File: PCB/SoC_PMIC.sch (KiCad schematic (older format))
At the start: 1 part

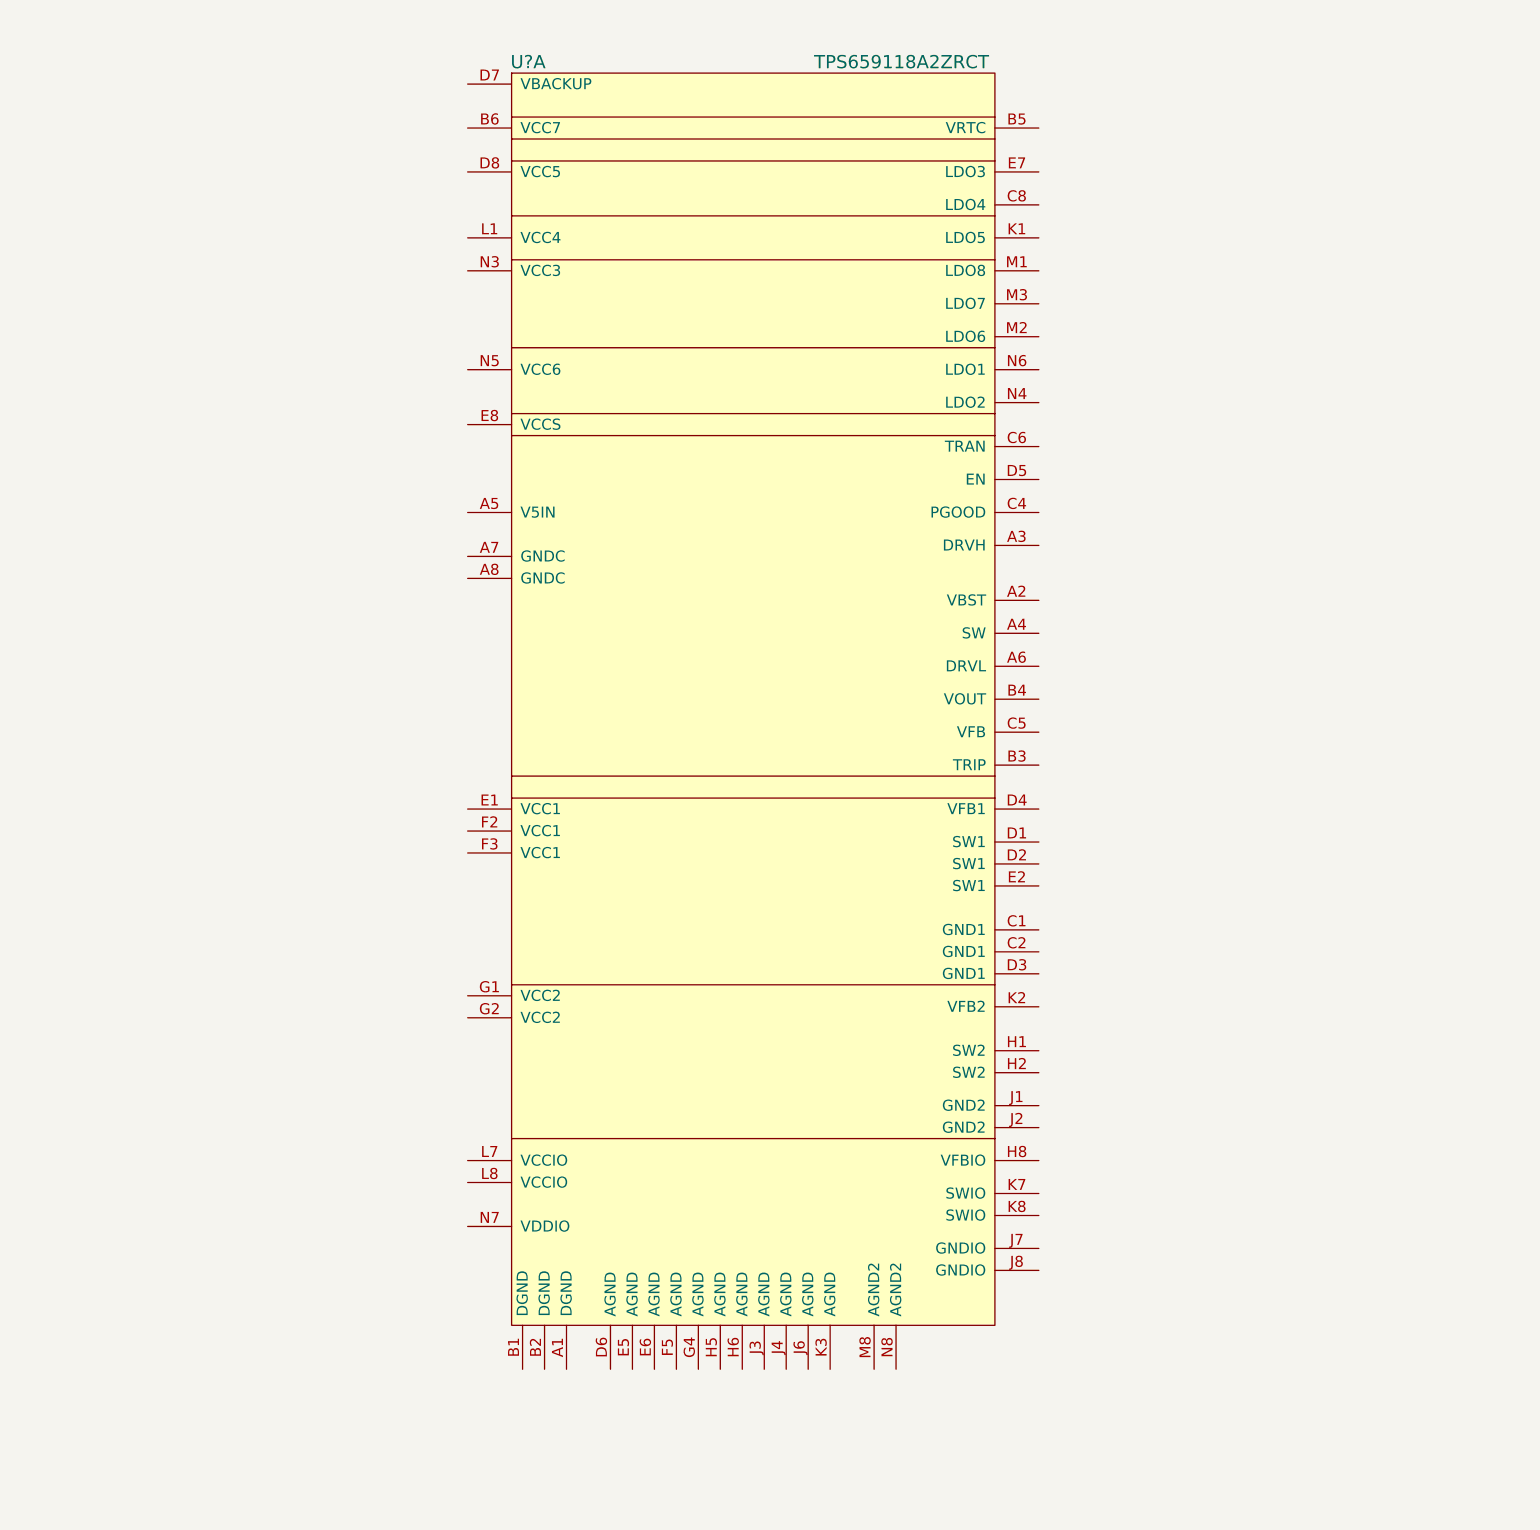
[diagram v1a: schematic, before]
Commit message: Cam / PMIC
Camera data bus entry relabled, PMIC started.
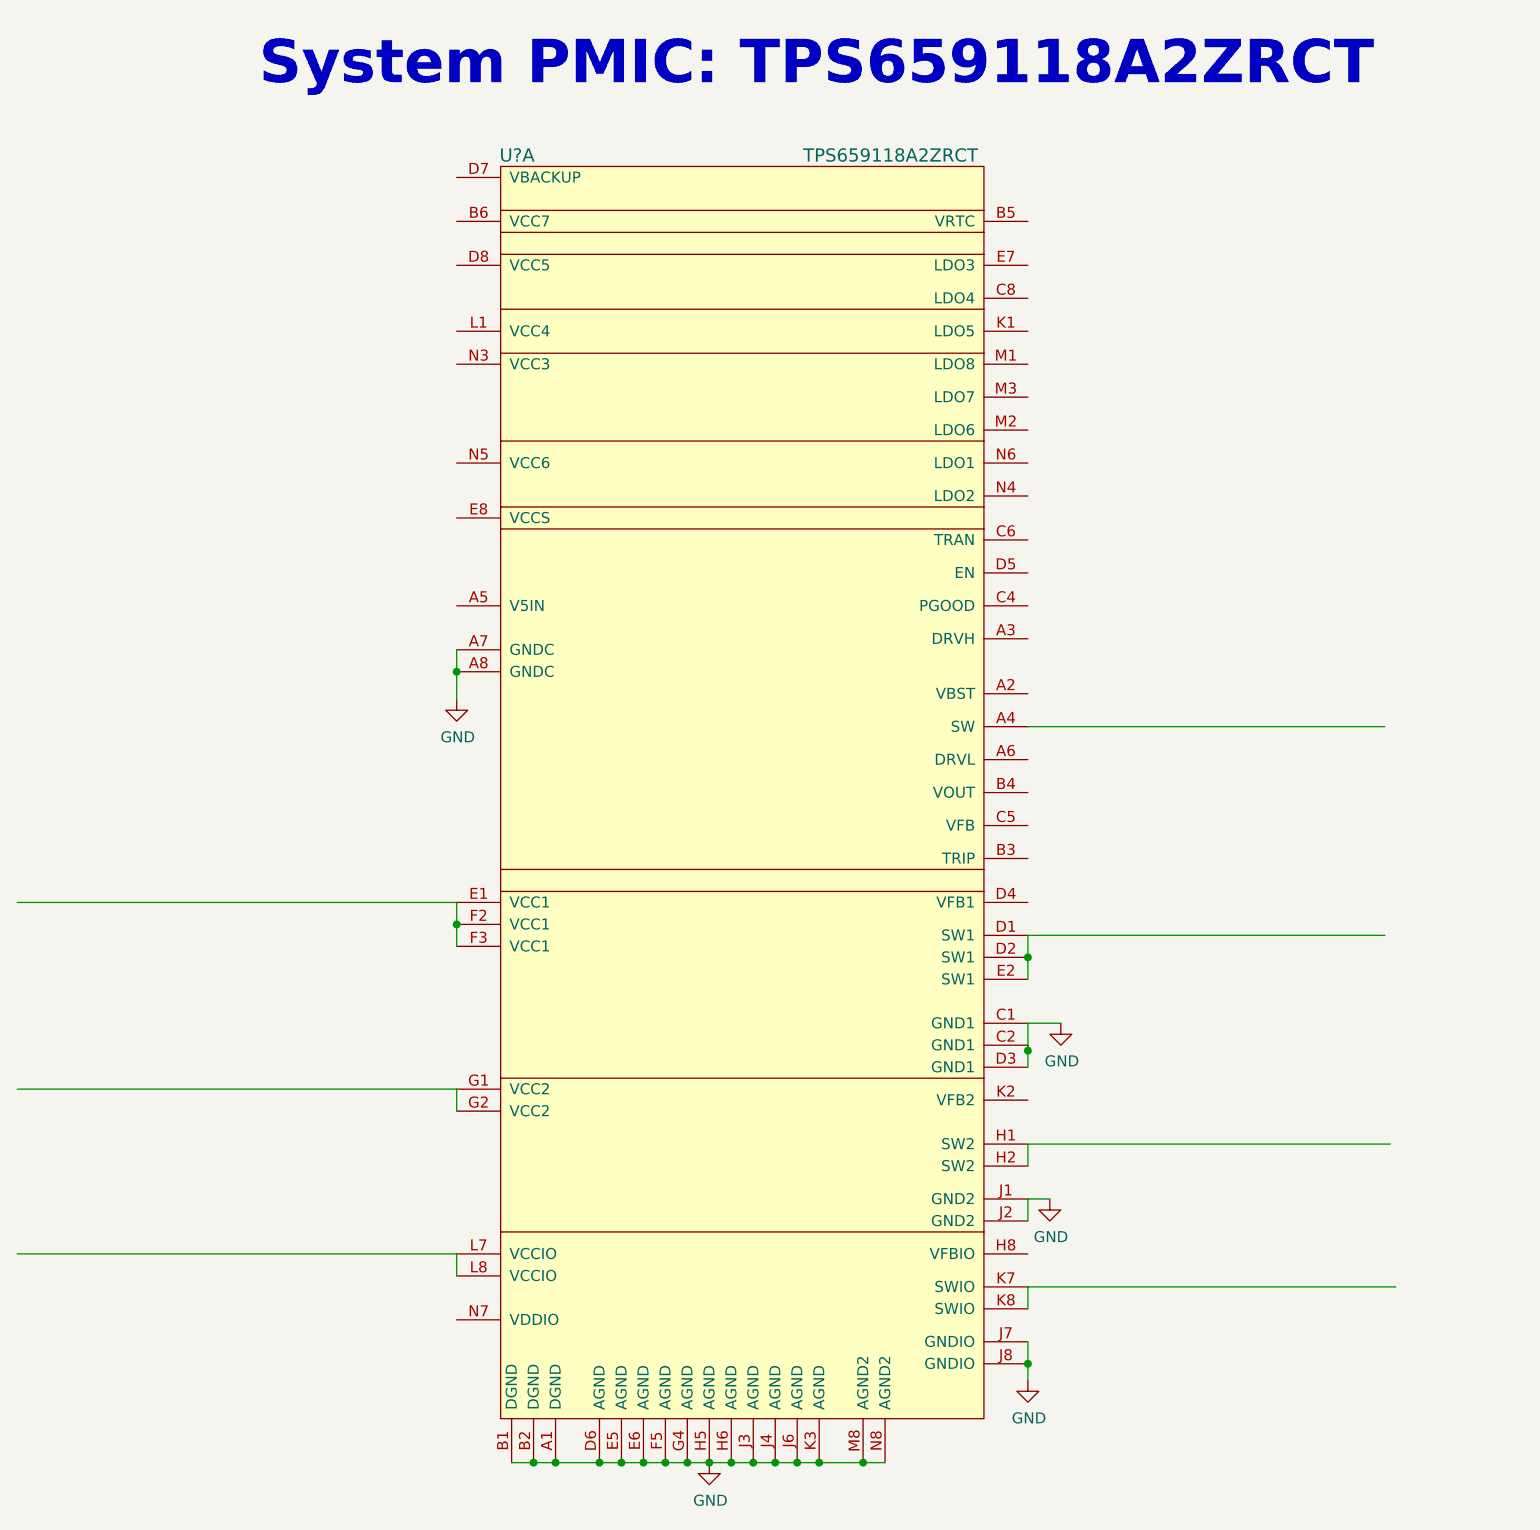
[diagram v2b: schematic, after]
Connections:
- net labels added: GND
- wire segments 0 -> 21
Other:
- note added: "System PMIC: TPS659118A2ZRCT"
- moved on the sheet: U?A
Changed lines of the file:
@@
 L TPS659118A2ZRCT U?
 U 1 1 58787CF1
-P 5625 3675
-F 0 "U?" H 4600 6625 60  0000 C CNN
-F 1 "TPS659118A2ZRCT" H 6300 6625 60  0000 C CNN
-F 2 "PCB_Footprints:TPS659118A2ZRCT" H 6250 8450 60  0001 C CNN
-F 3 "http://www.ti.com/lit/ds/symlink/tps65911.pdf" H 6450 8575 60  0001 C CNN
-F 4 "9.51000" H 4675 6725 60  0001 C CNN "Cost"
-F 5 "12 Jan 2017" H 4775 6825 60  0001 C CNN "Date Created"
-F 6 "12 Jan 2017" H 4875 6925 60  0001 C CNN "Date Modified"
-F 7 "Adam Vadala-Roth" H 4975 7025 60  0001 C CNN "Designer"
-F 8 "0.77mm" H 5075 7125 60  0001 C CNN "Height"
-F 9 "Yes" H 5175 7225 60  0001 C CNN "RhoS?"
-F 10 "Texas Instruments" H 5275 7325 60  0001 C CNN "MFR"
-F 11 "TPS659118A2ZRCT" H 5375 7425 60  0001 C CNN "MFR#"
-F 12 "SMT/SMD" H 5475 7525 60  0001 C CNN "Mounting"
-F 13 "98" H 5575 7625 60  0001 C CNN "Pin Count#"
-F 14 "Active" H 5675 7725 60  0001 C CNN "Status"
-F 15 "N/A" H 5775 7825 60  0001 C CNN "Tolerance"
-F 16 "IC PMIC DC/DC LDO 98BGA" H 5875 7925 60  0001 C CNN "Type"
-F 17 "2.7-5.5V" H 5975 8025 60  0001 C CNN "Voltage"
-F 18 "N/A" H 6075 8125 60  0001 C CNN "Wattage"
-F 19 "N/A" H 6175 8225 60  0001 C CNN "Component-Value"
-F 20 "Portable Equipment PMIC 98-BGA Microstar JR" H 6275 8325 60  0001 C CNN "Description"
-	1    5625 3675
+P 5575 4100
+F 0 "U?" H 4550 7050 60  0000 C CNN
+F 1 "TPS659118A2ZRCT" H 6250 7050 60  0000 C CNN
+F 2 "PCB_Footprints:TPS659118A2ZRCT" H 6200 8875 60  0001 C CNN
+F 3 "http://www.ti.com/lit/ds/symlink/tps65911.pdf" H 6400 9000 60  0001 C CNN
+F 4 "9.51000" H 4625 7150 60  0001 C CNN "Cost"
+F 5 "12 Jan 2017" H 4725 7250 60  0001 C CNN "Date Created"
+F 6 "12 Jan 2017" H 4825 7350 60  0001 C CNN "Date Modified"
+F 7 "Adam Vadala-Roth" H 4925 7450 60  0001 C CNN "Designer"
+F 8 "0.77mm" H 5025 7550 60  0001 C CNN "Height"
+F 9 "Yes" H 5125 7650 60  0001 C CNN "RhoS?"
+F 10 "Texas Instruments" H 5225 7750 60  0001 C CNN "MFR"
+F 11 "TPS659118A2ZRCT" H 5325 7850 60  0001 C CNN "MFR#"
+F 12 "SMT/SMD" H 5425 7950 60  0001 C CNN "Mounting"
+F 13 "98" H 5525 8050 60  0001 C CNN "Pin Count#"
+F 14 "Active" H 5625 8150 60  0001 C CNN "Status"
+F 15 "N/A" H 5725 8250 60  0001 C CNN "Tolerance"
+F 16 "IC PMIC DC/DC LDO 98BGA" H 5825 8350 60  0001 C CNN "Type"
+F 17 "2.7-5.5V" H 5925 8450 60  0001 C CNN "Voltage"
+F 18 "N/A" H 6025 8550 60  0001 C CNN "Wattage"
+F 19 "N/A" H 6125 8650 60  0001 C CNN "Component-Value"
+F 20 "Portable Equipment PMIC 98-BGA Microstar JR" H 6225 8750 60  0001 C CNN "Description"
+	1    5575 4100
 	1    0    0    -1
 $EndComp
+Wire Wire Line
+	4525 7100 6225 7100
+Connection ~ 4625 7100
+Connection ~ 4725 7100
+Connection ~ 4925 7100
+Connection ~ 5025 7100
+Connection ~ 5125 7100
+Connection ~ 5225 7100
+Connection ~ 5325 7100
+Connection ~ 5425 7100
+Connection ~ 5525 7100
+Connection ~ 5625 7100
+Connection ~ 5725 7100
+Connection ~ 5825 7100
+Connection ~ 5925 7100
+Connection ~ 6125 7100
+Wire Wire Line
+	6875 6550 6875 6725
+Wire Wire Line
+	6875 6000 6875 5900
+Wire Wire Line
+	6875 5200 6875 5300
+Wire Wire Line
+	6875 5225 6875 5100
+Connection ~ 6875 5225
+Wire Wire Line
+	4275 3400 4275 3625
+$Comp
+L GND #PWR?
+U 1 1 587D03A3
+P 5425 7100
+F 0 "#PWR?" H 5425 6850 50  0001 C CNN
+F 1 "GND" H 5430 6927 50  0000 C CNN
+F 2 "" H 5425 7100 50  0000 C CNN
+F 3 "" H 5425 7100 50  0000 C CNN
+	1    5425 7100
+	1    0    0    -1
+$EndComp
+$Comp
+L GND #PWR?
+U 1 1 587D03CF
+P 6875 6725
+F 0 "#PWR?" H 6875 6475 50  0001 C CNN
+F 1 "GND" H 6880 6552 50  0000 C CNN
+F 2 "" H 6875 6725 50  0000 C CNN
+F 3 "" H 6875 6725 50  0000 C CNN
+	1    6875 6725
+	1    0    0    -1
+$EndComp
+Connection ~ 6875 6650
+$Comp
+L GND #PWR?
+U 1 1 587D040E
+P 6975 5900
+F 0 "#PWR?" H 6975 5650 50  0001 C CNN
+F 1 "GND" H 6980 5727 50  0000 C CNN
+F 2 "" H 6975 5900 50  0000 C CNN
+F 3 "" H 6975 5900 50  0000 C CNN
+	1    6975 5900
+	1    0    0    -1
+$EndComp
+Wire Wire Line
+	6875 5900 6975 5900
+$Comp
+L GND #PWR?
+U 1 1 587D0455
+P 7025 5100
+F 0 "#PWR?" H 7025 4850 50  0001 C CNN
+F 1 "GND" H 7030 4927 50  0000 C CNN
+F 2 "" H 7025 5100 50  0000 C CNN
+F 3 "" H 7025 5100 50  0000 C CNN
+	1    7025 5100
+	1    0    0    -1
+$EndComp
+Wire Wire Line
+	6875 5100 7025 5100
+$Comp
+L GND #PWR?
+U 1 1 587D04A5
+P 4275 3625
+F 0 "#PWR?" H 4275 3375 50  0001 C CNN
+F 1 "GND" H 4280 3452 50  0000 C CNN
+F 2 "" H 4275 3625 50  0000 C CNN
+F 3 "" H 4275 3625 50  0000 C CNN
+	1    4275 3625
+	1    0    0    -1
+$EndComp
+Connection ~ 4275 3500
+Wire Wire Line
+	6875 5750 6875 5650
+Wire Wire Line
+	6875 5650 8525 5650
+Wire Wire Line
+	6875 6300 6875 6400
+Wire Wire Line
+	6875 6300 8550 6300
+Wire Wire Line
+	6875 4700 6875 4900
+Connection ~ 6875 4800
+Wire Wire Line
+	6875 4700 8500 4700
+Wire Wire Line
+	6875 3750 8500 3750
+Text Notes 3375 850  0    197  ~ 39
+System PMIC: TPS659118A2ZRCT
+Wire Wire Line
+	4275 4550 4275 4750
+Connection ~ 4275 4650
+Wire Wire Line
+	4275 5400 4275 5500
+Wire Wire Line
+	4275 6150 4275 6250
+Wire Wire Line
+	4275 6150 2275 6150
+Wire Wire Line
+	4275 5400 2275 5400
+Wire Wire Line
+	4275 4550 2275 4550
 $EndSCHEMATC

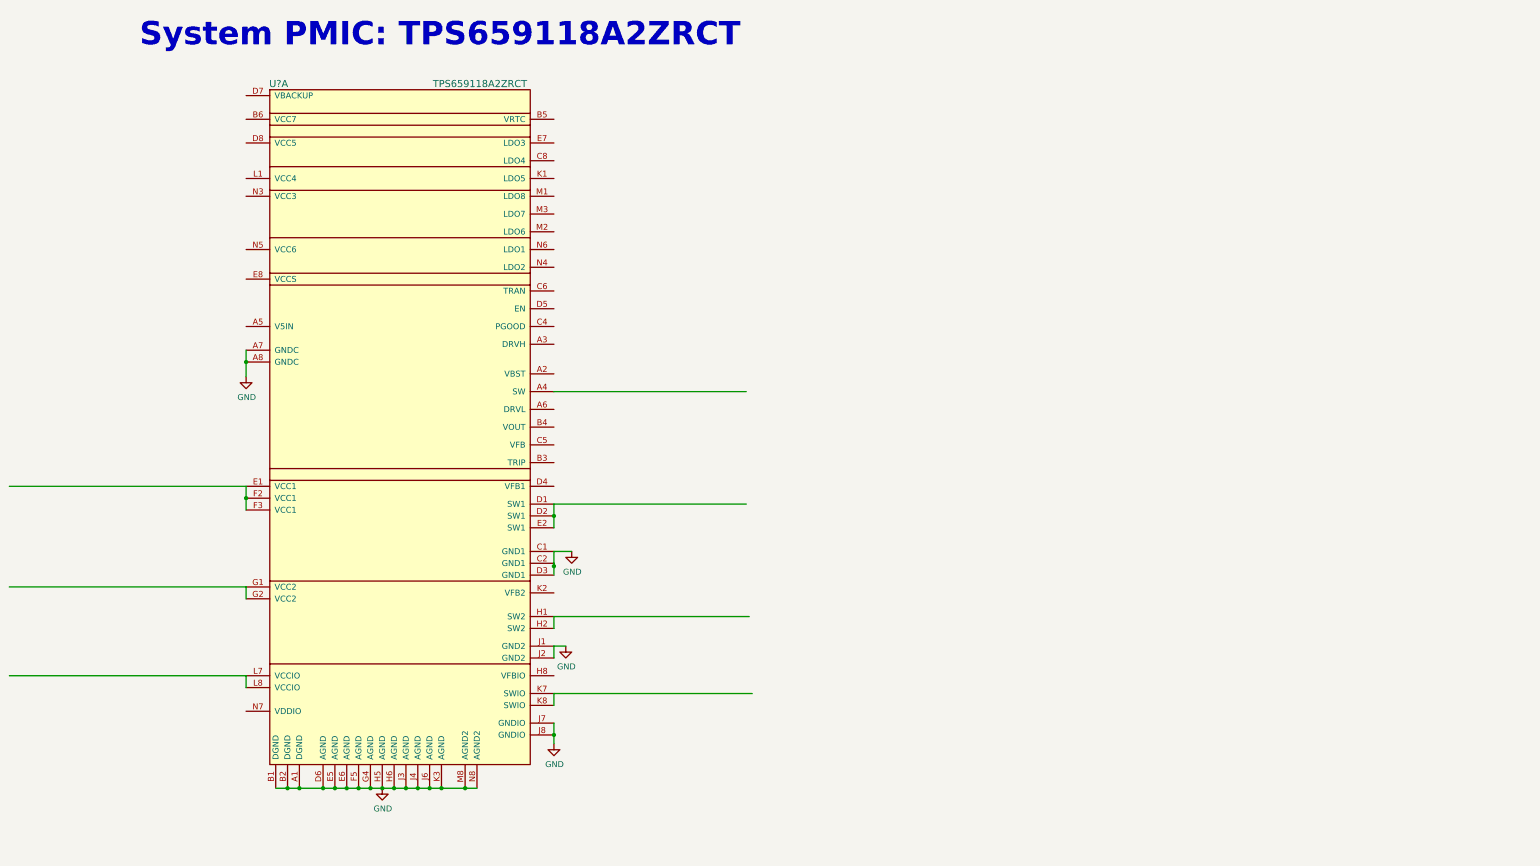
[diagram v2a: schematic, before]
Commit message: PMIC
PMIC components chosen with symbols/footprints all created. See
hydroPWNics footprints lib for details. Currently working on PMIC
schematic everything else comes next.
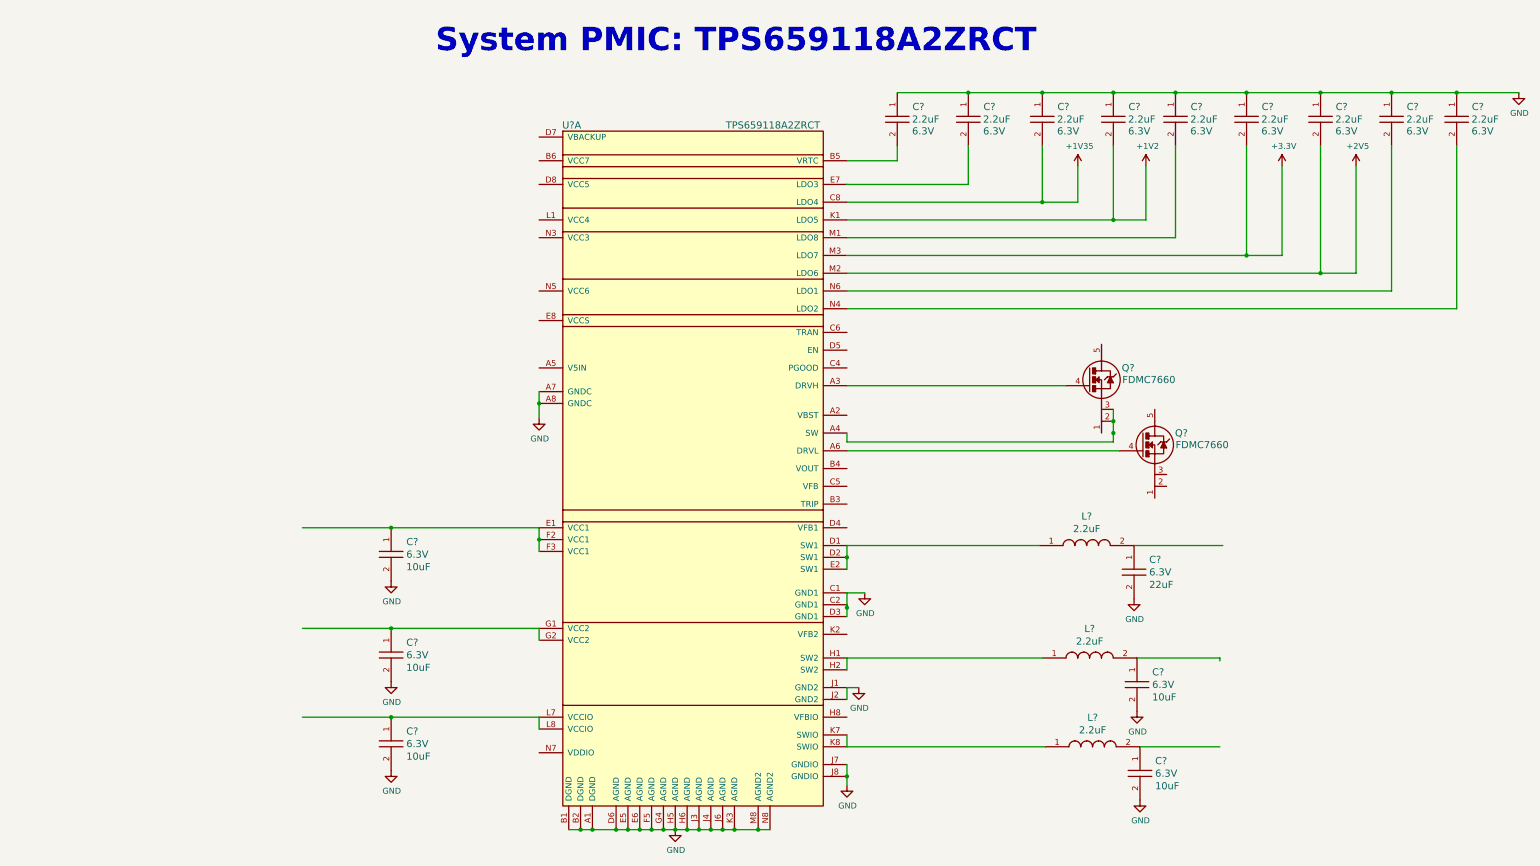
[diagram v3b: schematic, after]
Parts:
- added C? (x9): CL10A225KQ8NNNC, PCB_Footprints:C0603, symbol CL10A225KQ8NNNC
- added C? (x5): CL21A106KAFN3NE, PCB_Footprints:C0805, symbol CL21A106KAFN3NE
- added C?: CL10A226KQ8NRNE, PCB_Footprints:C0603, symbol CL10A226KQ8NRNE
- added L? (x3): VLCF5020T-2R2N2R6-3, PCB_Footprints:VLCF5020T-2R2N2R6-3, symbol VLCF5020T-2R2N2R6-3
- added Q? (x2): FDMC7660, PCB_Footprints:FDMC7660, symbol FDMC7660
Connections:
- net labels added: +1V2, +1V35, +2V5, +3.3V
- wire segments 21 -> 89
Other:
- moved on the sheet: U?A
